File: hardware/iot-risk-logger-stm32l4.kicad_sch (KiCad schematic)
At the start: 50 parts, among them J2 Conn_ST_STDC14, J3 USB Type-C, Q1 IRLML6401, U1 STM32L412K8Tx, U2 MMA8452QR1, U3 ST25DV04K, U4 OPT3001DNPR, U5 SHT30-DIS, U6 AT25SF041B-SSHD-T, U7 L78L33ABUTR, Y1 SC-32S32.768

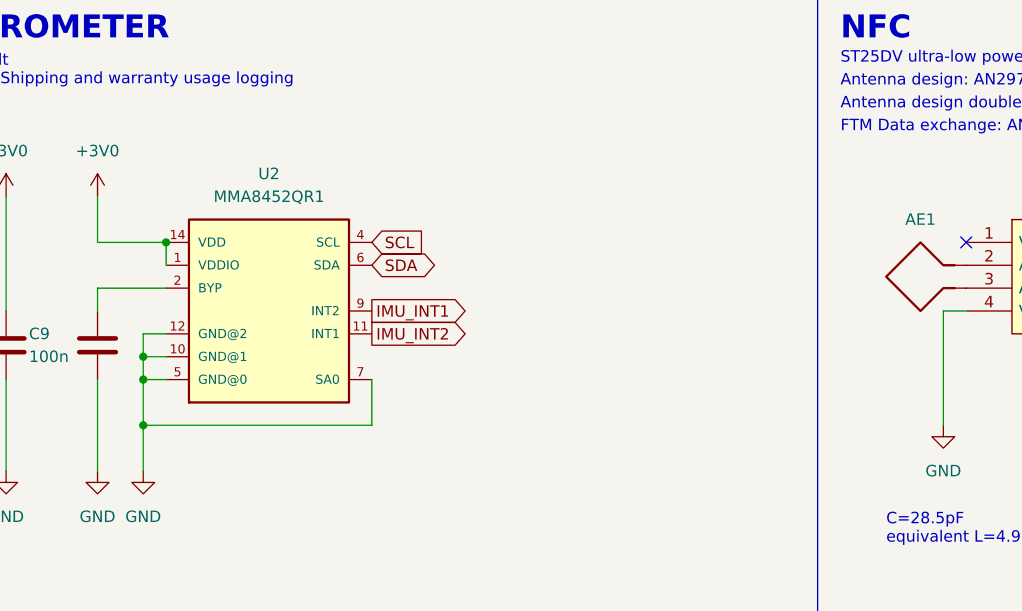
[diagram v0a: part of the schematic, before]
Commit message: rename to iot-risk-logger-stm32l4 and andd harwware/
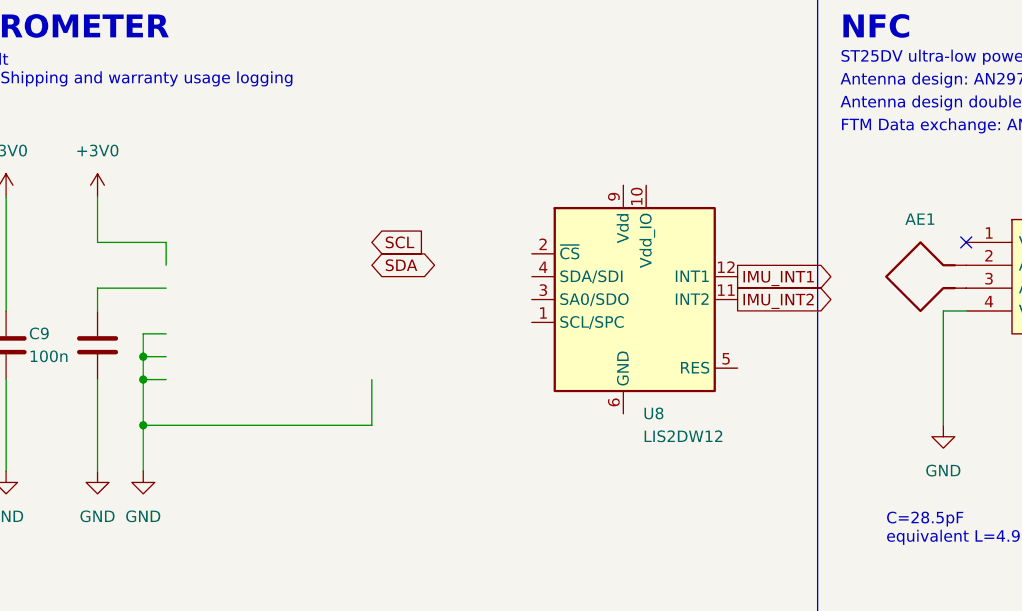
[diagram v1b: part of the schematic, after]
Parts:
- removed U2: MMA8452QR1, Personal:XDCR_MMA8452QR1, symbol MMA8452Q:MMA8452Q
- added U8: LIS2DW12, Package_LGA:LGA-12_2x2mm_P0.5mm, symbol Sensor_Motion:LIS2DE12
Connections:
- net IMU_INT1: now also U8.12 (INT1)
- net IMU_INT2: now also U8.11 (INT2)
- new net: U8.6 (GND), U8.7 (GND), U8.8 (GND)
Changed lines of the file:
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@@
   (junction (at 147.32 196.85) (diameter 0) (color 0 0 0 0)
-  )
-  (junction (at 64.77 40.64) (diameter 0) (color 0 0 0 0)
   )
   (junction (at 226.06 243.84) (diameter 0) (color 0 0 0 0)
@@
     )
   )
-  (global_label "IMU_INT1" (shape output) (at 87.63 48.26 0) (fields_autoplaced)
-    (effects (font (size 1.27 1.27)) (justify left))
-    (property "Intersheetrefs" "${INTERSHEET_REFS}" (at 98.5098 48.1806 0)
-      (effects (font (size 1.27 1.27)) (justify left) hide)
-    )
-  )
   (global_label "SDA" (shape bidirectional) (at 87.63 212.09 0) (fields_autoplaced)
     (effects (font (size 1.27 1.27)) (justify left))
@@
     )
   )
+  (global_label "IMU_INT1" (shape output) (at 128.27 44.45 0) (fields_autoplaced)
+    (effects (font (size 1.27 1.27)) (justify left))
+    (property "Intersheetrefs" "${INTERSHEET_REFS}" (at 139.1498 44.3706 0)
+      (effects (font (size 1.27 1.27)) (justify left) hide)
+    )
+  )
   (global_label "_LED" (shape output) (at 36.83 224.79 180) (fields_autoplaced)
     (effects (font (size 1.27 1.27)) (justify right))
@@
     )
   )
-  (global_label "IMU_INT2" (shape output) (at 87.63 50.8 0) (fields_autoplaced)
-    (effects (font (size 1.27 1.27)) (justify left))
-    (property "Intersheetrefs" "${INTERSHEET_REFS}" (at 98.5098 50.7206 0)
-      (effects (font (size 1.27 1.27)) (justify left) hide)
-    )
-  )
   (global_label "TEMP_INT" (shape output) (at 359.41 53.34 0) (fields_autoplaced)
     (effects (font (size 1.27 1.27)) (justify left))
     (property "Intersheetrefs" "${INTERSHEET_REFS}" (at 370.5317 53.2606 0)
+      (effects (font (size 1.27 1.27)) (justify left) hide)
+    )
+  )
+  (global_label "IMU_INT2" (shape output) (at 128.27 46.99 0) (fields_autoplaced)
+    (effects (font (size 1.27 1.27)) (justify left))
+    (property "Intersheetrefs" "${INTERSHEET_REFS}" (at 139.1498 46.9106 0)
       (effects (font (size 1.27 1.27)) (justify left) hide)
     )
@@
         (path "/a430d7dc-28bf-48df-bb1e-9c942d21db4d"
           (reference "C3") (unit 1)
+        )
+      )
+    )
+  )
+  (symbol (lib_id "Sensor_Motion:LIS2DE12") (at 115.57 46.99 0) (unit 1)
+    (in_bom yes) (on_board yes) (dnp no) (fields_autoplaced)
+    (property "Reference" "U8" (at 117.7641 59.69 0)
+      (effects (font (size 1.27 1.27)) (justify left))
+    )
+    (property "Value" "LIS2DW12" (at 117.7641 62.23 0)
+      (effects (font (size 1.27 1.27)) (justify left))
+    )
+    (property "Footprint" "Package_LGA:LGA-12_2x2mm_P0.5mm" (at 119.38 33.02 0)
+      (effects (font (size 1.27 1.27)) (justify left) hide)
+    )
+    (property "Datasheet" "https://datasheet.lcsc.com/lcsc/1810010032_STMicroelectronics-LIS2DW12TR_C189624.pdf" (at 106.68 46.99 0)
+      (effects (font (size 1.27 1.27)) hide)
+    )
+    (property "LCSC Part" "C189624" (at 115.57 46.99 0)
+      (effects (font (size 1.27 1.27)) hide)
+    )
+    (property "URL" "https://www.lcsc.com/product-detail/Attitude-Sensor-Gyroscope_STMicroelectronics-LIS2DW12TR_C189624.html" (at 115.57 46.99 0)
+      (effects (font (size 1.27 1.27)) hide)
+    )
+    (property "Part" "LIS2DW12TR" (at 115.57 46.99 0)
+      (effects (font (size 1.27 1.27)) hide)
+    )
+    (pin "4")
+    (pin "1")
+    (pin "9")
+    (pin "7")
+    (pin "10")
+    (pin "5")
+    (pin "6")
+    (pin "3")
+    (pin "2")
+    (pin "8")
+    (pin "11")
+    (pin "12")
+    (instances
+      (project "iot-risk-data-logger-saml11"
+        (path "/a0c78d85-b3f6-4318-9ed0-83640f187f18"
+          (reference "U8") (unit 1)
         )
       )
@@
         )
       )
-    )
-  )
-  (symbol (lib_id "MMA8452Q:MMA8452Q") (at 74.93 48.26 0) (unit 1)
-    (in_bom yes) (on_board yes) (dnp no) (fields_autoplaced)
-    (property "Reference" "U2" (at 76.2 33.02 0)
-      (effects (font (size 1.27 1.27)))
-    )
-    (property "Value" "MMA8452QR1" (at 76.2 35.56 0)
-      (effects (font (size 1.27 1.27)))
-    )
-    (property "Footprint" "Personal:XDCR_MMA8452QR1" (at 74.93 48.26 0)
-      (effects (font (size 1.27 1.27)) hide)
-    )
-    (property "Datasheet" "https://datasheet.lcsc.com/lcsc/1806121726_NXP-Semicon-MMA8452QR1_C11360.pdf" (at 74.93 48.26 0)
-      (effects (font (size 1.27 1.27)) hide)
-    )
-    (property "LCSC Part" "C11360" (at 74.93 48.26 0)
-      (effects (font (size 1.27 1.27)) hide)
-    )
-    (property "URL" "https://www.lcsc.com/product-detail/Attitude-Sensor-Gyroscope_NXP-Semicon-MMA8452QR1_C11360.html" (at 74.93 48.26 0)
-      (effects (font (size 1.27 1.27)) hide)
-    )
-    (property "Part" "MMA8452QR1" (at 74.93 48.26 0)
-      (effects (font (size 1.27 1.27)) hide)
-    )
-    (pin "1")
-    (pin "10")
-    (pin "11")
-    (pin "12")
-    (pin "14")
-    (pin "2")
-    (pin "4")
-    (pin "5")
-    (pin "6")
-    (pin "7")
-    (pin "9")
-    (instances
-      (project "iot-risk-data-logger-saml11"
-        (path "/a0c78d85-b3f6-4318-9ed0-83640f187f18"
-          (reference "U2") (unit 1)
-        )
-      )
-      (project "iot-data-logger-nfc-samd21"
-        (path "/a430d7dc-28bf-48df-bb1e-9c942d21db4d"
-          (reference "U7") (unit 1)
-        )
-      )

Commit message: CubeMX: draft initial config, KiCad: pins assignment draft
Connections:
- net XIN32 is gone; now on net OSC32_IN: C17.1, Y1.1
- net XOUT32 is gone; now on net OSC32_OUT: C18.1, Y1.2
- net MISO: now also U1.12 (PA6)
- net MOSI: now also U1.13 (PA7)
- net SCK: now also U1.11 (PA5)
- net SCL: now also U1.19 (PA9), U8.1 (SCL/SPC)
- net SDA: now also U1.20 (PA10), U8.4 (SDA/SDI)
- net USB_DM: now also U1.21 (PA11)
- net USB_DP: now also U1.22 (PA12)
- net USB_VBUS_SENSE: now also U1.8 (PA2)
- net _FLASH_CS: now also U1.14 (PB0)
- net _NFC_INT: now also U1.6 (PA0)
- net OSC32_IN: now reaches U1.2 (PC14)
- net OSC32_OUT: now reaches U1.3 (PC15)
- no-connect marks 19 -> 16
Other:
- note added: "System WakeUp pins: PA0, PA2 work in the Shutdown mode with ~18nA consumption"
- note added: "TODO: should I add pullup on NFC? No internal pullups allowed Same for USB VBUS, pins are floating in Shutdown mode"
- note added: "TODO: verify 22p caps"
- note removed: "MOSI - SERCOM 1/PAD[0] SCK - SERCOM 1/PAD[1] _FLASH_CS - SERCOM 1/PAD[2] MISO - SERCOM 1/PAD[3]"
- note removed: "PICKIT"
- note removed: "SDA - SERCOM 0/PAD[0] SCL - SERCOM 0/PAD[1]"
- note removed: "TODO: now it has name LSE instead of XOSC, verify 22p caps"

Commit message: CubeMX: set pins
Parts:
- removed C1: 100n, Capacitor_SMD:C_0805_2012Metric_Pad1.18x1.45mm_HandSolder, symbol Device:C
- removed J2: Conn_ST_STDC14, Connector_PinHeader_1.27mm:PinHeader_2x07_P1.27mm_Vertical_SMD, symbol Connector:Conn_ST_STDC14
- removed R1: 1k, Resistor_SMD:R_0805_2012Metric_Pad1.20x1.40mm_HandSolder, symbol Device:R
- added J1: Conn_ARM_JTAG_SWD_10, Connector_PinHeader_1.27mm:PinHeader_2x05_P1.27mm_Vertical, symbol Connector:Conn_ARM_JTAG_SWD_10
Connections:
- net +3V0: now also J1.1 (VTref)
- net GND: now also J1.3 (GND), J1.5 (GND), J1.9 (GNDDetect)
- net IMU_INT1: now also U1.9 (PA3)
- net IMU_INT2: now also U1.10 (PA4)
- net SWDCLK: now also U1.24 (PA14), J1.4 (SWCLK/TCK)
- net SWDIO: now also U1.23 (PA13), J1.2 (SWDIO/TMS)
- net SWO: now also U1.26 (PB3), J1.6 (SWO/TDO)
- net TEMP_INT: now also U1.28 (PB5)
- net _LED: now also U1.15 (PB1)
- net _LIGHT_INT: now also U1.7 (PA1)
- net _RESET: now also J1.10 (~{RESET})
- net _TEMP_RESET: now also U1.27 (PB4)
- net DEBUG_TX: now reaches U1.29 (PB6)
- net DEBUG_RX: now reaches U1.30 (PB7)
- no-connect marks 16 -> 7
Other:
- note added: "TODO: Add 2x05 1,27 component LCSC"
- note removed: "System WakeUp pins: PA0, PA2 work in the Shutdown mode with ~18nA consumption"
- note removed: "TODO check internal pull-up and +3V3 connection"
- note removed: "TODO: should I add pullup on NFC? No internal pullups allowed Same for USB VBUS, pins are floating in Shutdown mode"
- moved on the sheet: U8

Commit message: CubeMX: add qspi
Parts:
- removed C16: 100n, Capacitor_SMD:C_0805_2012Metric_Pad1.18x1.45mm_HandSolder, symbol Device:C
- removed F1: MSMF010 0.01A, Fuse:Fuse_1812_4532Metric_Pad1.30x3.40mm_HandSolder, symbol Device:Polyfuse
- removed TP3: TestPoint_Probe, TestPoint:TestPoint_THTPad_D1.5mm_Drill0.7mm, symbol Connector:TestPoint_Probe
- removed U6: AT25SF041B-SSHD-T, Package_SO:SOIC-8_3.9x4.9mm_P1.27mm, symbol AT25DF041B-XMHN-B:AT25DF041B-XMHN-B
- added H1, H2: MountingHole, MountingHole:MountingHole_3.2mm_M3_ISO14580_Pad_TopBottom, symbol Mechanical:MountingHole
- added R1: 33k, Resistor_SMD:R_0805_2012Metric_Pad1.20x1.40mm_HandSolder, symbol Device:R
- added U2: W25Q64JV, Package_SO:SOIC-8_5.23x5.23mm_P1.27mm, symbol Memory_Flash:W25Q32JVSS
- C15: value 22u -> 100n; footprint Capacitor_SMD:C_1206_3216Metric_Pad1.33x1.80mm_HandSolder -> Capacitor_SMD:C_0805_2012Metric_Pad1.18x1.45mm_HandSolder; LCSC Part C12891 -> C1711; Part CL31A226KAHNNNE -> CL21B104KBCNNNC; URL https://www.lcsc.com/product-detail/Multilayer-Ceramic-Capacitors-MLCC-SMD-SMT_Samsung-Electro-Mechanics-CL31A226KAHNNNE_C12891.html -> https://www.lcsc.com/product-detail/Multilayer-Ceramic-Capacitors-MLCC-SMD-SMT_Samsung-Electro-Mechanics-CL21B104KBCNNNC_C1711.html
- C3, C9: value 100n -> 1u; LCSC Part C1711 -> C2932475; Part CL21B104KBCNNNC -> CL21A105KACLNNC; URL https://www.lcsc.com/product-detail/Multilayer-Ceramic-Capacitors-MLCC-SMD-SMT_Samsung-Electro-Mechanics-CL21B104KBCNNNC_C1711.html -> https://www.lcsc.com/product-detail/Multilayer-Ceramic-Capacitors-MLCC-SMD-SMT_span-style-background-color-ff0-Samsung-span-span-style-background-color-ff0-Electro-Mechanics-span-CL21A105KACLNNC_C2932475.html
- J1: footprint Connector_PinHeader_1.27mm:PinHeader_2x05_P1.27mm_Vertical -> Connector:Tag-Connect_TC2050-IDC-NL_2x05_P1.27mm_Vertical_with_bottom_clip
- R4, R5: value 4k7 -> 5k1; LCSC Part C60816 -> C84375; Part RC0805FR-074K7L -> RC0805FR-075K1L; URL https://www.lcsc.com/product-detail/Chip-Resistor-Surface-Mount_YAGEO-RC0805FR-074K7L_C60816.html -> https://www.lcsc.com/product-detail/Chip-Resistor-Surface-Mount_YAGEO-RC0805FR-075K1L_C84375.html
- R6: LCSC Part C84376 -> (none); Part RC0805FR-0710KL -> (none); URL https://www.lcsc.com/product-detail/Chip-Resistor-Surface-M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 -> (none)
- R9: value 10k -> 82k; LCSC Part C84376 -> (none); Part RC0805FR-0710KL -> (none); URL https://www.lcsc.com/product-detail/Chip-Resistor-Surface-M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 -> (none)
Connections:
- net DEBUG_RX is gone; now on net IMU_INT2: U1.30 (PB7)
- net DEBUG_TX is gone; now on net IMU_INT1: U1.29 (PB6)
- net VDDCODE is gone; now on net VDDA: C10.1, C8.1
- net +3V0: now also C4.1, C6.1, C7.1, C9.1, R6.1, U1.1 (VDD), U1.17 (VDD), U8.10 (Vdd_IO), U8.9 (Vdd), U2.8 (VCC); no longer C15.1
- net +5V: now also R9.1; no longer R6.1
- net GND: now also U8.5 (RES), U8.6 (GND), U8.7 (GND), U8.8 (GND), R1.2, U2.4 (GND); no longer R9.2
- net IMU_INT1: no longer U1.9 (PA3)
- net IMU_INT2: no longer U1.10 (PA4)
- net SCL: now also R4.2; no longer R5.2
- net SDA: now also R5.2; no longer R4.2
- net USB_VBUS_SENSE: now also R9.2, U1.18 (PA8), R1.1; no longer R6.2, R9.1, U1.8 (PA2)
- net _LED: now also U1.25 (PA15); no longer U1.15 (PB1)
- net _RESET: now also C15.1
- net at Q1.3 (D): now also BT1.1 (+)
- net VDDA: now reaches U1.5 (VDDA)
- net VDDA: now also FB1.2
- net MISO renamed QSPI_IO3
- net QSPI_IO3: now also U2.7 (IO3)
- net MOSI renamed QSPI_IO2
- net QSPI_IO2: now also U2.3 (IO2)
- net OSC32_IN: no longer names the net of C17.1, U1.2 (PC14), Y1.1
- net OSC32_OUT: no longer names the net of C18.1, U1.3 (PC15), Y1.2
- net SCK: no longer names the net of U1.11 (PA5)
- removed net VDDANA: C4.1, C6.1, FB1.2
- net _FLASH_CS renamed QSPI_IO1
- net QSPI_IO1: now also U2.2 (DO(IO1))
- new net QSPI_CLK: U1.9 (PA3), U2.6 (CLK)
- new net QSPI_IO0: U1.15 (PB1), U2.5 (DI(IO0))
- new net _QSPI_NCS: R6.2, U1.8 (PA2), U2.1 (~{CS})
- no-connect marks 7 -> 9
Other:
- note added: "QSPI NOR FLASH 8MB"
- note added: "TODO: find on LCSC"
- note added: "W25Q works down to 2V7, better to be 2V4"
- note removed: "0.5Mb, works down to 2V5"
- note removed: "NOR FLASH"
- note removed: "Power: Linear Mode Only"
- note removed: "TODO: check _RESET 100n cap"
- note removed: "TODO: verify 22p caps"
- moved on the sheet: AE1, BT1, C10, C14, C17, C18, C4, C6, C7, C8, FB1, Q1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

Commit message: PCB: first version of layout
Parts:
- removed TP1, TP2: TestPoint_Probe, TestPoint:TestPoint_THTPad_D1.5mm_Drill0.7mm, symbol Connector:TestPoint_Probe
- U5: renamed from U7; footprint Package_TO_SOT_SMD:SOT-89-3_Handsoldering -> Package_TO_SOT_SMD:SOT-89-3
- renumbered C9 to C1, C19 to C10, C8 to C11, C10 to C12, C7 to C13, C4 to C14, C6 to C15, C17 to C16, C18 to C17, C15 to C18, C11 to C2, C12 to C3, C13 to C4, C2 to C6, C3 to C7, C20 to C8, C14 to C9, D2 to D1, D1 to D2, J3 to J1, J1 to J2, R7 to R1, R8 to R2, R5 to R4, R4 to R5, R2 to R7, R9 to R8, R1 to R9, U3 to U1, U4 to U2, U5 to U3, U8 to U4, U2 to U6, U1 to U7

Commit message: Schematics: assign all BOM parts
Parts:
- removed C12: 1u, Capacitor_SMD:C_0805_2012Metric_Pad1.18x1.45mm_HandSolder, symbol Device:C
- removed C16, C17: 22p, Capacitor_SMD:C_0805_2012Metric_Pad1.18x1.45mm_HandSolder, symbol Device:C
- removed D2: LED, LED_SMD:LED_0805_2012Metric_Pad1.15x1.40mm_HandSolder, symbol Device:LED
- removed H1, H2: MountingHole, MountingHole:MountingHole_3.2mm_M3_ISO14580_Pad_TopBottom, symbol Mechanical:MountingHole
- removed J2: Conn_ARM_JTAG_SWD_10, Connector:Tag-Connect_TC2050-IDC-NL_2x05_P1.27mm_Vertical_with_bottom_clip, symbol Connector:Conn_ARM_JTAG_SWD_10
- removed R3: 1k, Resistor_SMD:R_0805_2012Metric_Pad1.20x1.40mm_HandSolder, symbol Device:R
- removed R6: 10k, Resistor_SMD:R_0805_2012Metric_Pad1.20x1.40mm_HandSolder, symbol Device:R
- removed U5: L78L33ABUTR, Package_TO_SOT_SMD:SOT-89-3, symbol Regulator_Linear:L78L33_SOT89
- removed U6: W25Q64JV, Package_SO:SOIC-8_5.23x5.23mm_P1.27mm, symbol Memory_Flash:W25Q32JVSS
- added C10 (x2): 22p, Capacitor_SMD:C_0603_1608Metric, symbol Device:C
- added D5: LED, LED_SMD:LED_0805_2012Metric_Pad1.15x1.40mm_HandSolder, symbol Device:LED
- added J5: TagConnect SWD ARM, Connector:Tag-Connect_TC2050-IDC-NL_2x05_P1.27mm_Vertical_with_bottom_clip, symbol Connector:Conn_ARM_JTAG_SWD_10
- added R15: 1k, Resistor_SMD:R_0805_2012Metric_Pad1.20x1.40mm_HandSolder, symbol Device:R
- added R19 (x2): 10k, Resistor_SMD:R_0603_1608Metric_Pad0.98x0.95mm_HandSolder, symbol Device:R
- added U3: W25Q64JV, Package_SO:SOIC-8_5.23x5.23mm_P1.27mm, symbol Memory_Flash:W25Q32JVSS
- added U5: AP2112K-3.3, Package_TO_SOT_SMD:SOT-23-5, symbol Regulator_Linear:AP2112K-3.3
- AE1: footprint footprints:ANT_NFC_30x40 -> RF_Antenna:NFC_20x40
- BT1: LCSC Part C964829 -> (none); LCSC Part # (none) -> C964829; LCSC URL (none) -> https://www.lcsc.com/product-detail/Battery-Connectors_MYOU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; Manufacturer (none) -> MYOUNG; Mfr. Part # (none) -> MY-2032-05; Part MY-2032-05 -> (none); URL https://www.lcsc.com/product-detail/Battery-Connectors_MYOU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 -> (none)
- C1, C7: value 1u -> 10u; LCSC Part C2932475 -> (none); LCSC Part # (none) -> C1713; LCSC URL (none) -> https://www.lcsc.com/product-detail/Multilayer-Ceramic-Capa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; Manufacturer (none) -> Samsung Electro-Mechanics; Mfr. Part # (none) -> CL21A106KOQNNNE; Part CL21A105KACLNNC -> (none); URL https://www.lcsc.com/product-detail/Multilayer-Ceramic-Capa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 -> (none)
- C10: footprint Capacitor_SMD:C_0805_2012Metric_Pad1.18x1.45mm_HandSolder -> Capacitor_SMD:C_0603_1608Metric_Pad1.08x0.95mm_HandSolder; LCSC Part C50131 -> (none); LCSC Part # (none) -> C1621; LCSC URL (none) -> https://www.lcsc.com/product-detail/Multilayer-Ceramic-Capa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; Manufacturer (none) -> Samsung Electro-Mechanics; Mfr. Part # (none) -> CL10B472KB8NNNC; Part CL21B472KBANNNC -> (none); URL https://www.lcsc.com/product-detail/Multilayer-Ceramic-Capa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 -> (none)
- C11, C13, C14, C18, C2, C3, C4, C6, C9: footprint Capacitor_SMD:C_0805_2012Metric_Pad1.18x1.45mm_HandSolder -> Capacitor_SMD:C_0603_1608Metric_Pad1.08x0.95mm_HandSolder; LCSC Part C1711 -> (none); LCSC Part # (none) -> C1591; LCSC URL (none) -> https://www.lcsc.com/product-detail/Multilayer-Ceramic-Capa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; Manufacturer (none) -> Samsung Electro-Mechanics; Mfr. Part # (none) -> CL10B104KB8NNNC; Part CL21B104KBCNNNC -> (none); URL https://www.lcsc.com/product-detail/Multilayer-Ceramic-Capa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 -> (none)
- C15: value 10u -> 100n; footprint Capacitor_SMD:C_0805_2012Metric_Pad1.18x1.45mm_HandSolder -> Capacitor_SMD:C_0603_1608Metric_Pad1.08x0.95mm_HandSolder; LCSC Part C1713 -> (none); LCSC Part # (none) -> C1591; LCSC URL (none) -> https://www.lcsc.com/product-detail/Multilayer-Ceramic-Capa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; Manufacturer (none) -> Samsung Electro-Mechanics; Mfr. Part # (none) -> CL10B104KB8NNNC; Part CL21A106KOQNNNE -> (none); URL https://www.lcsc.com/product-detail/Multilayer-Ceramic-Capa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 -> (none)
- C5, C8: LCSC Part C1713 -> (none); LCSC Part # (none) -> C1713; LCSC URL (none) -> https://www.lcsc.com/product-detail/Multilayer-Ceramic-Capa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; Manufacturer (none) -> Samsung Electro-Mechanics; Mfr. Part # (none) -> CL21A106KOQNNNE; Part CL21A106KOQNNNE -> (none); URL https://www.lcsc.com/product-detail/Multilayer-Ceramic-Capa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 -> (none)
- D1: LCSC Part C5355496 -> (none); LCSC Part # (none) -> C5355496; LCSC URL (none) -> https://www.lcsc.com/product-detail/Schottky-Barrier-Diodes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; Manufacturer (none) -> Infineon; Mfr. Part # (none) -> BAT60A; Part BAT60A -> (none); URL https://www.lcsc.com/product-detail/Schottky-Barrier-Diodes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 -> (none)
- D3: LCSC Part C2827688 -> (none); LCSC Part # (none) -> C2827688; LCSC URL (none) -> https://www.lcsc.com/product-detail/ESD-Protection-Devices_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; Manufacturer (none) -> TECH PUBLIC; Mfr. Part # (none) -> PRTR5V0U2X; Part PRTR5V0U2X -> (none); URL https://www.lcsc.com/product-detail/ESD-Protection-Devices_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 -> (none)
- FB1: LCSC Part C47130 -> (none); LCSC Part # (none) -> C47130; LCSC URL (none) -> https://www.lcsc.com/product-detail/Ferrite-Beads_Murata-El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; Manufacturer (none) -> Murata; Mfr. Part # (none) -> BLM21PG331SN1D; Part BLM21PG331SN1D -> (none); URL https://www.lcsc.com/product-detail/Ferrite-Beads_Murata-El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 -> (none)
- J1: LCSC Part C709357 -> (none); LCSC Part # (none) -> C709357; LCSC URL (none) -> https://www.lcsc.com/product-detail/USB-Connectors_Shenzhen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; Manufacturer (none) -> Shenzhen Kinghelm Elec; Mfr. Part # (none) -> KH-TYPE-C-16P; Part KH-TYPE-C-16P -> (none); URL https://www.lcsc.com/product-detail/USB-Connectors_Shenzhen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 -> (none)
- Q1: LCSC Part C3034 -> (none); LCSC Part # (none) -> C3034; LCSC URL (none) -> https://www.lcsc.com/product-detail/MOSFETs_Infineon-Techno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; Manufacturer (none) -> Infineon; Mfr. Part # (none) -> IRLML6401TRPBF; Part IRLML6401TRPBF -> (none); URL https://www.lcsc.com/product-detail/MOSFETs_Infineon-Techno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 -> (none)
- R1, R2, R4, R5: footprint Resistor_SMD:R_0805_2012Metric_Pad1.20x1.40mm_HandSolder -> Resistor_SMD:R_0603_1608Metric_Pad0.98x0.95mm_HandSolder; LCSC Part C84375 -> (none); LCSC Part # (none) -> C14677; LCSC URL (none) -> https://www.lcsc.com/product-detail/Chip-Resistor-Surface-M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; Manufacturer (none) -> YAGEO; Mfr. Part # (none) -> RC0603JR-075K1L; Part RC0805FR-075K1L -> (none); URL https://www.lcsc.com/product-detail/Chip-Resistor-Surface-M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 -> (none)
- R7: footprint Resistor_SMD:R_0805_2012Metric_Pad1.20x1.40mm_HandSolder -> Resistor_SMD:R_0603_1608Metric_Pad0.98x0.95mm_HandSolder; LCSC Part C107700 -> (none); LCSC Part # (none) -> C107698; LCSC URL (none) -> https://www.lcsc.com/product-detail/Chip-Resistor-Surface-M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; Manufacturer (none) -> YAGEO; Mfr. Part # (none) -> RC0603JR-071ML; Part RC0805FR-071ML -> (none); URL https://www.lcsc.com/product-detail/Chip-Resistor-Surface-M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 -> (none)
- R8: footprint Resistor_SMD:R_0805_2012Metric_Pad1.20x1.40mm_HandSolder -> Resistor_SMD:R_0603_1608Metric_Pad0.98x0.95mm_HandSolder; LCSC Part # (none) -> C137678; LCSC URL (none) -> https://www.lcsc.com/product-detail/Chip-Resistor-Surface-M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; Manufacturer (none) -> YAGEO; Mfr. Part # (none) -> RC0603FR-0782KL
- R9: footprint Resistor_SMD:R_0805_2012Metric_Pad1.20x1.40mm_HandSolder -> Resistor_SMD:R_0603_1608Metric_Pad0.98x0.95mm_HandSolder; LCSC Part # (none) -> C126359; LCSC URL (none) -> https://www.lcsc.com/product-detail/Chip-Resistor-Surface-M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; Manufacturer (none) -> YAGEO; Mfr. Part # (none) -> RC0603FR-0733KL
- U1: LCSC Part C2654816 -> (none); LCSC Part # (none) -> C2654816; LCSC URL (none) -> https://www.lcsc.com/product-detail/RF-Chips_STMicroelectro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; Mfr. Part # (none) -> ST25DV04K-IER6T3; Part ST25DV04K-IER6T3 -> (none); URL https://www.lcsc.com/product-detail/RF-Chips_STMicroelectro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 -> (none)
- U2: LCSC Part C90462 -> (none); LCSC Part # (none) -> C90462; LCSC URL (none) -> https://www.lcsc.com/product-detail/Ambient-Light-Sensors_T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; Mfr. Part # (none) -> OPT3001DNPR; Part OPT3001DNPR -> (none); URL https://www.lcsc.com/product-detail/Ambient-Light-Sensors_T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 -> (none)
- U3: LCSC Part C2687423 -> (none); LCSC Part # (none) -> C2687423; LCSC URL (none) -> https://www.lcsc.com/product-detail/Temperature-and-Humidit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; Manufacturer (none) -> Sensirion; Mfr. Part # (none) -> SHT30-DIS-B10KS; Part SHT30-DIS-B10KS -> (none); URL https://www.lcsc.com/product-detail/Temperature-and-Humidit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 -> (none)
- U4: LCSC Part C189624 -> (none); LCSC Part # (none) -> C189624; LCSC URL (none) -> https://www.lcsc.com/product-detail/Attitude-Sensor-Gyrosco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; Manufacturer (none) -> STMicroelectronics; Mfr. Part # (none) -> LIS2DW12TR; Part LIS2DW12TR -> (none); URL https://www.lcsc.com/product-detail/Attitude-Sensor-Gyrosco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 -> (none)
- U7: value STM32L412K8Tx -> STM32L412; LCSC Part # (none) -> C529438; LCSC URL (none) -> https://www.lcsc.com/product-detail/Microcontroller-Units-M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; Manufacturer (none) -> STMicroelectronics; Mfr. Part # (none) -> STM32L412KBT6
- Y1: value SC-32S32.768 -> 32.768; footprint Crystal:Crystal_SMD_EuroQuartz_EQ161-2Pin_3.2x1.5mm_HandSoldering -> Crystal:Crystal_SMD_EuroQuartz_EQ161-2Pin_3.2x1.5mm; LCSC Part C97606 -> (none); LCSC Part # (none) -> C97606; LCSC URL (none) -> https://www.lcsc.com/product-detail/Crystals_Seiko-SC-32S32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; Manufacturer (none) -> Seiko; Mfr. Part # (none) -> SC-32S32.768kHz20PPM12.5pF; Part SC-32S32.768kHz20PPM12.5pF -> (none); URL https://www.lcsc.com/product-detail/Crystals_Seiko-SC-32S32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 -> (none)
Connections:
- net +3V0: now also C18.1, J5.1 (VTref), R15.1, R19.2, U3.8 (VCC), U5.5 (VOUT); no longer C13.1, C14.1, C15.1, C7.1, U7.1 (VDD), U7.17 (VDD)
- net +5V: now also U5.1 (VIN), U5.3 (EN)
- net GND: now also C10.2, C10.2, J5.3 (GND), J5.5 (GND), J5.9 (GNDDetect), R19.1, U3.4 (GND), U5.2 (GND)
- net QSPI_CLK: now also U3.6 (CLK)
- net QSPI_IO0: now also U3.5 (DI(IO0))
- net QSPI_IO1: now also U3.2 (DO(IO1))
- net QSPI_IO2: now also U3.3 (IO2)
- net QSPI_IO3: now also U3.7 (IO3)
- net SWDCLK: now also J5.4 (SWCLK/TCK)
- net SWDIO: now also J5.2 (SWDIO/TMS)
- net SWO: now also J5.6 (SWO/TDO)
- net _LED: now also D5.1 (K)
- net _QSPI_NCS: now also R19.1, U3.1 (~{CS})
- net _RESET: now also C15.1, J5.10 (~{RESET}); no longer C18.1
- net GND_SHIELD: now reaches C10.1, D3.1 (GND), J1.S1 (SHIELD), R7.1
- net +BATTERY: now reaches BT1.1 (+), Q1.3 (D)
- net CC1: now reaches J1.A5 (CC1), R1.2
- net LSE_OUT: now reaches U7.3 (PC15), Y1.2
- net LSE_OUT: now also C10.1
- net LSE_IN: now reaches U7.2 (PC14), Y1.1
- net LSE_IN: now also C10.1
- net BOOT0: now reaches U7.31 (PH3)
- net BOOT0: now also R19.2
- net +VBUS: now reaches D1.2 (A), J1.A4 (VBUS), J1.A9 (VBUS), J1.B4 (VBUS), J1.B9 (VBUS)
- net CC2: now reaches J1.B5 (CC2), R2.2
- net USB_DM renamed USB_N
- net USB_DP renamed USB_P
- net VDDA renamed VDD
- net VDD: now also C13.1, C14.1, C7.1, U7.1 (VDD), U7.17 (VDD)
- new net +LED: D5.2 (A), R15.2
- no-connect marks 9 -> 8
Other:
- note added: "0x44, ADDR=L"
- note added: "Cload = 12p5 Cstray =~ 1p CX1 = CX2 = 2(12.5p - 1p) =~ 22p"
- note added: "I = 1mA"
- note added: "I2C 0x??, ADDR=GND"
- note added: "LDO, Udrop = 250mV"
- note removed: "Current: ~1mA"
- note removed: "TODO: Add 2x05 1,27 component LCSC"
- note removed: "TODO: USB-C connector has mounting pins. The footprint should be updated accordingly."
- note removed: "TODO: find on LCSC"
- moved on the sheet: BT1, C5, C6, D1, D3, FB1, Q1, R4, R8, R9, U4, U7

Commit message: PCB: prefinal board
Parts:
- added TP1: TP: SDA, TestPoint:TestPoint_THTPad_D1.5mm_Drill0.7mm, symbol Connector:TestPoint_Probe
- added TP2: TP: SCL, TestPoint:TestPoint_THTPad_D1.5mm_Drill0.7mm, symbol Connector:TestPoint_Probe
- added TP3: TP: GND, TestPoint:TestPoint_THTPad_D1.5mm_Drill0.7mm, symbol Connector:TestPoint_Probe
- added TP4: TP: NFC_INT, TestPoint:TestPoint_THTPad_D1.5mm_Drill0.7mm, symbol Connector:TestPoint_Probe
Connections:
- net +3V0: no longer C1.1, C18.1, C2.1, C3.1, C4.1, C5.1, C6.1, C9.1, J5.1 (VTref), R15.1, R19.2, R4.1, R5.1, U1.8 (VCC), U2.1 (VDD), U3.5 (VDD), U3.8 (VCC), U4.10 (Vdd_IO), U4.9 (Vdd)
- net GND: now also TP3.1
- net SCL: now also TP2.1
- net SDA: now also TP1.1
- net VDD: now also C1.1, C18.1, C2.1, C3.1, C4.1, C5.1, C6.1, C9.1, J5.1 (VTref), R15.1, R19.2, R4.1, R5.1, U1.8 (VCC), U2.1 (VDD), U3.5 (VDD), U3.8 (VCC), U4.10 (Vdd_IO), U4.9 (Vdd)
- net _NFC_INT: now also TP4.1
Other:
- note added: "ARM SWD"
- note added: "BATTERY & PROTECTION & OR"
- note added: "I2C PULL-UPS"
- note added: "LDO: 5V -> 3V3"
- note added: "LED"
- note added: "LOW-PASS FILTER"
- note added: "MCU CAPS"
- note added: "Q1 works as a reverse polarity protection, closes on 5V presence from USB (Ugate > Usource)"
- note added: "USB-C: POWER & MSD"
- note added: "W25Q works down to 2V7, better to replace by 2V4 memory"
- note removed: "POWER"
- note removed: "TODO: check AN4879 Ann note about STM USB"
- note removed: "W25Q works down to 2V7, better to be 2V4"
- title: (none) -> IoT Risk data logger
- moved on the sheet: AE1, BT1, C1, C10, C11, C13, C14, C15, C18, C2, C3, C4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
